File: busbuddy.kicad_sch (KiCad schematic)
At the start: 0 parts

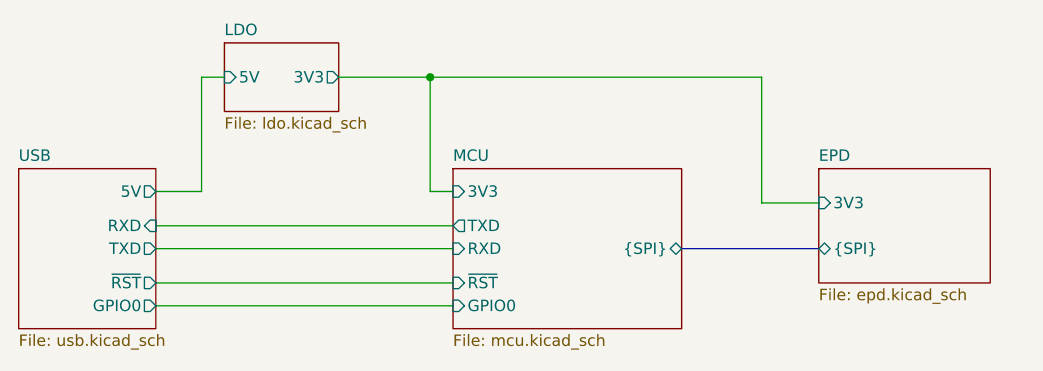
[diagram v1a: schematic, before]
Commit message: Correct SPI pinout
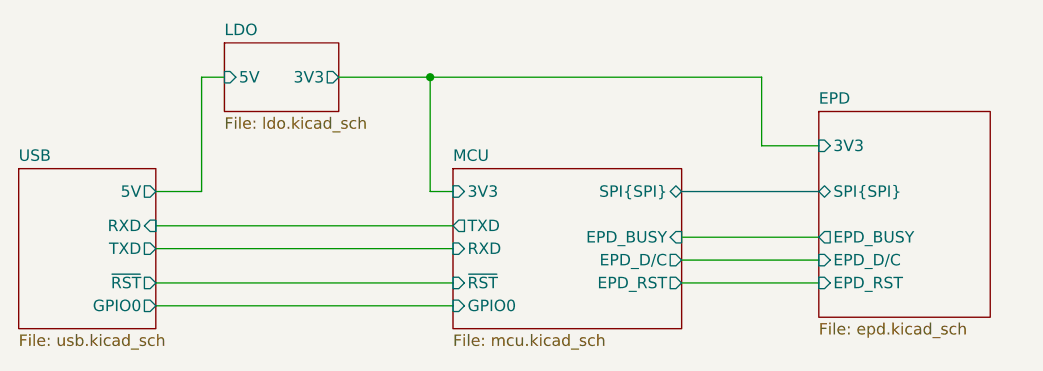
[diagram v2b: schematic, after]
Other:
- sheet EPD ports: added EPD_BUSY, EPD_D/C, EPD_RST, SPI{SPI}; removed {SPI}
- sheet MCU ports: added EPD_BUSY, EPD_D/C, EPD_RST, SPI{SPI}; removed {SPI}
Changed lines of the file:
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@@
 	(wire
 		(pts
-			(xy 127 43.18) (xy 127 57.15)
+			(xy 127 43.18) (xy 127 50.8)
+		)
+		(stroke
+			(width 0)
+			(type default)
+		)
+	)
+	(wire
+		(pts
+			(xy 90.17 43.18) (xy 80.01 43.18)
 		)
 		(stroke
@@
 	(bus
 		(pts
-			(xy 118.11 62.23) (xy 133.35 62.23)
-		)
-		(stroke
-			(width 0)
-			(type default)
-		)
-	)
-	(wire
-		(pts
-			(xy 90.17 43.18) (xy 80.01 43.18)
+			(xy 118.11 55.88) (xy 133.35 55.88)
+		)
+		(stroke
+			(width 0)
+			(type default)
+		)
+	)
+	(wire
+		(pts
+			(xy 118.11 66.04) (xy 133.35 66.04)
 		)
 		(stroke
@@
 	(wire
 		(pts
-			(xy 133.35 57.15) (xy 127 57.15)
+			(xy 118.11 63.5) (xy 133.35 63.5)
+		)
+		(stroke
+			(width 0)
+			(type default)
+		)
+	)
+	(wire
+		(pts
+			(xy 133.35 50.8) (xy 127 50.8)
 		)
 		(stroke
@@
 		(pts
 			(xy 59.69 55.88) (xy 64.77 55.88)
+		)
+		(stroke
+			(width 0)
+			(type default)
+		)
+	)
+	(wire
+		(pts
+			(xy 118.11 60.96) (xy 133.35 60.96)
 		)
 		(stroke
@@
 			)
 		)
-		(pin "{SPI}" bidirectional
-			(at 118.11 62.23 0)
+		(pin "SPI{SPI}" bidirectional
+			(at 118.11 55.88 0)
 			(effects
 				(font
@@
 				)
 				(justify left)
+			)
+		)
+		(pin "EPD_BUSY" input
+			(at 118.11 60.96 0)
+			(effects
+				(font
+					(size 1.27 1.27)
+				)
+				(justify right)
+			)
+		)
+		(pin "EPD_D{slash}C" output
+			(at 118.11 63.5 0)
+			(effects
+				(font
+					(size 1.27 1.27)
+				)
+				(justify right)
+			)
+		)
+		(pin "EPD_RST" output
+			(at 118.11 66.04 0)
+			(effects
+				(font
+					(size 1.27 1.27)
+				)
+				(justify right)
 			)
 		)
@@
 	)
 	(sheet
-		(at 133.35 53.34)
-		(size 19.05 12.7)
+		(at 133.35 46.99)
+		(size 19.05 22.86)
 		(fields_autoplaced yes)
 		(stroke
@@
 		)
 		(property "Sheetname" "EPD"
-			(at 133.35 52.6284 0)
+			(at 133.35 46.2784 0)
 			(effects
 				(font
@@
 		)
 		(property "Sheetfile" "epd.kicad_sch"
-			(at 133.35 66.6246 0)
+			(at 133.35 70.4346 0)
 			(effects
 				(font
@@
 			)
 		)
-		(pin "{SPI}" bidirectional
-			(at 133.35 62.23 180)
+		(pin "SPI{SPI}" bidirectional
+			(at 133.35 55.88 180)
 			(effects
 				(font
@@
 		)
 		(pin "3V3" input
-			(at 133.35 57.15 180)
-			(effects
-				(font
+			(at 133.35 50.8 180)
+			(effects
+				(font
+					(size 1.27 1.27)
+				)
+				(justify left)
+			)
+		)
+		(pin "EPD_D{slash}C" input
+			(at 133.35 63.5 180)
+			(effects
+				(font
+					(size 1.27 1.27)
+				)
+				(justify left)
+			)
+		)
+		(pin "EPD_RST" input
+			(at 133.35 66.04 180)
+			(effects
+				(font
+					(size 1.27 1.27)
+				)
+				(justify left)
+			)
+		)
+		(pin "EPD_BUSY" output
+			(at 133.35 60.96 180)
+			(effects
+				(font

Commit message: Finish everything
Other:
- note added: "TX/RX flipped in USB sheet."
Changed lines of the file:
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@@
+	(wire
+		(pts
+			(xy 59.69 59.69) (xy 92.71 59.69)
+		)
+		(stroke
+			(width 0)
+			(type default)
+		)
+	)
 	(wire
 		(pts
@@
 	(wire
 		(pts
-			(xy 59.69 59.69) (xy 92.71 59.69)
-		)
-		(stroke
-			(width 0)
-			(type default)
-		)
-	)
-	(wire
-		(pts
 			(xy 90.17 55.88) (xy 90.17 43.18)
 		)
@@
 			(width 0)
 			(type default)
+		)
+	)
+	(text "TX/RX flipped in USB sheet."
+		(exclude_from_sim no)
+		(at 76.2 58.42 0)
+		(effects
+			(font
+				(size 1.27 1.27)
+			)
 		)
 	)
@@
 		)
 		(pin "TXD" output
+			(at 59.69 59.69 0)
+			(effects
+				(font
+					(size 1.27 1.27)
+				)
+				(justify right)
+			)
+		)
+		(pin "RXD" input
 			(at 59.69 62.23 0)
 			(effects
 				(font
-					(size 1.27 1.27)
-				)
-				(justify right)
-			)
-		)
-		(pin "RXD" input
-			(at 59.69 59.69 0)
-			(effects
-				(font
